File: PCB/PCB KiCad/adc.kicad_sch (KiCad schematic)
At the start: 9 parts, among them U2 NAU7802SGI

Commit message: pre route
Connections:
- net DRDY_INT: no longer names the net of U2.12 (DRDY)
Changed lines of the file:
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@@
   (no_connect (at 163.83 109.22))
   (no_connect (at 163.83 106.68))
-  (wire (pts (xy 163.83 93.98) (xy 175.26 93.98))
-    (stroke (width 0) (type default))
-  )
   (wire (pts (xy 128.27 106.68) (xy 133.35 106.68))
     (stroke (width 0) (type default))
@@
     (stroke (width 0) (type default))
   )
-  (global_label "DRDY_INT" (shape input) (at 175.26 93.98 0) (fields_autoplaced)
-    (effects (font (size 1.27 1.27)) (justify left))
-    (property "Intersheetrefs" "${INTERSHEET_REFS}" (at 186.4421 93.9006 0)
-      (effects (font (size 1.27 1.27)) (justify left) hide)
-    )
-  )
   (global_label "SCL" (shape bidirectional) (at 170.18 99.06 0) (fields_autoplaced)

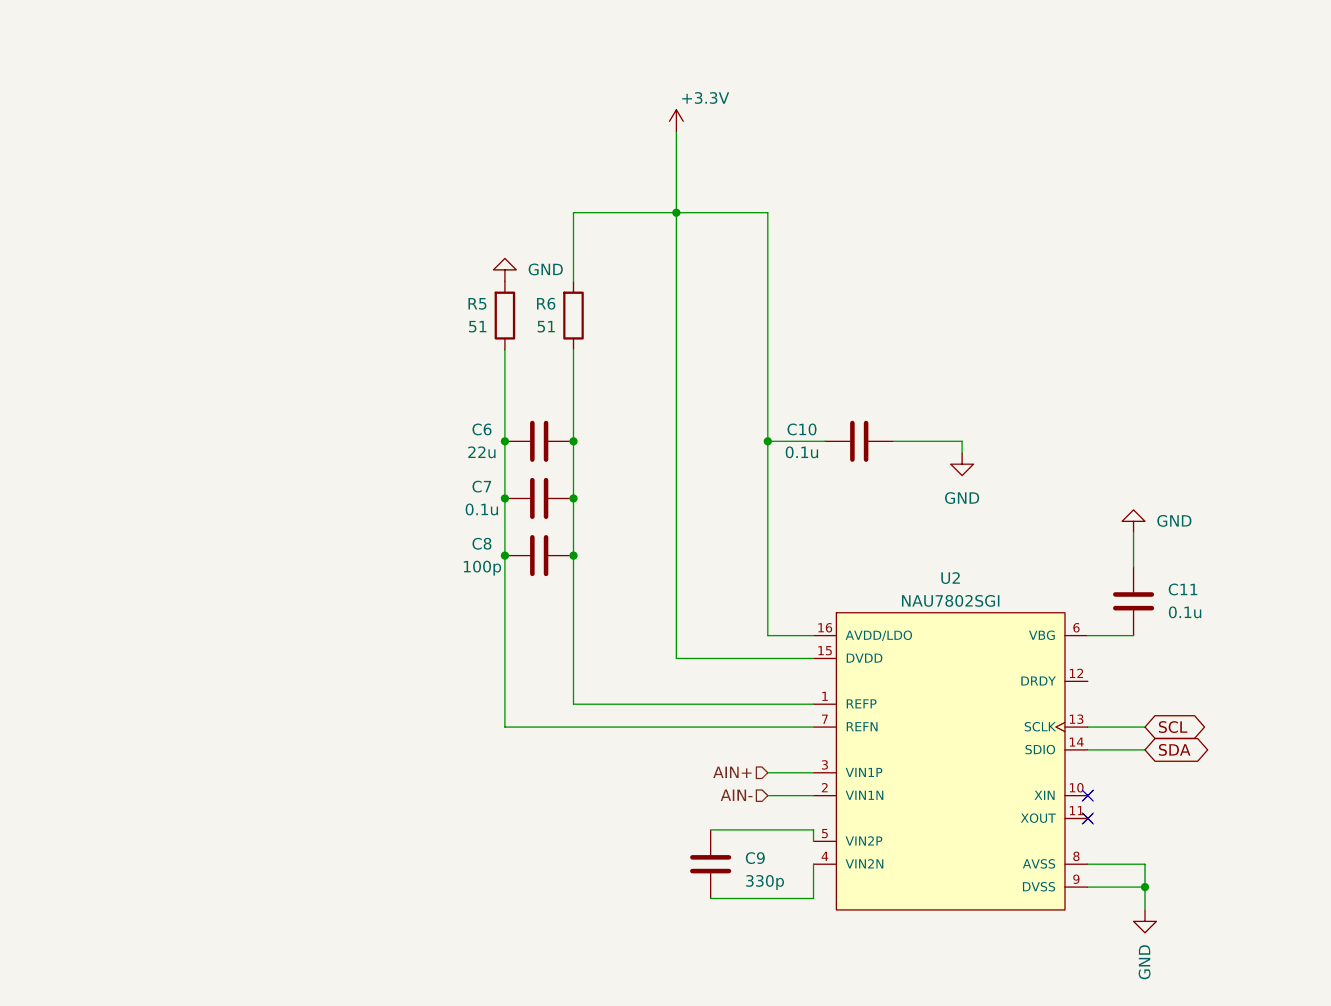
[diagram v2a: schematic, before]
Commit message: adds LP5951MFX
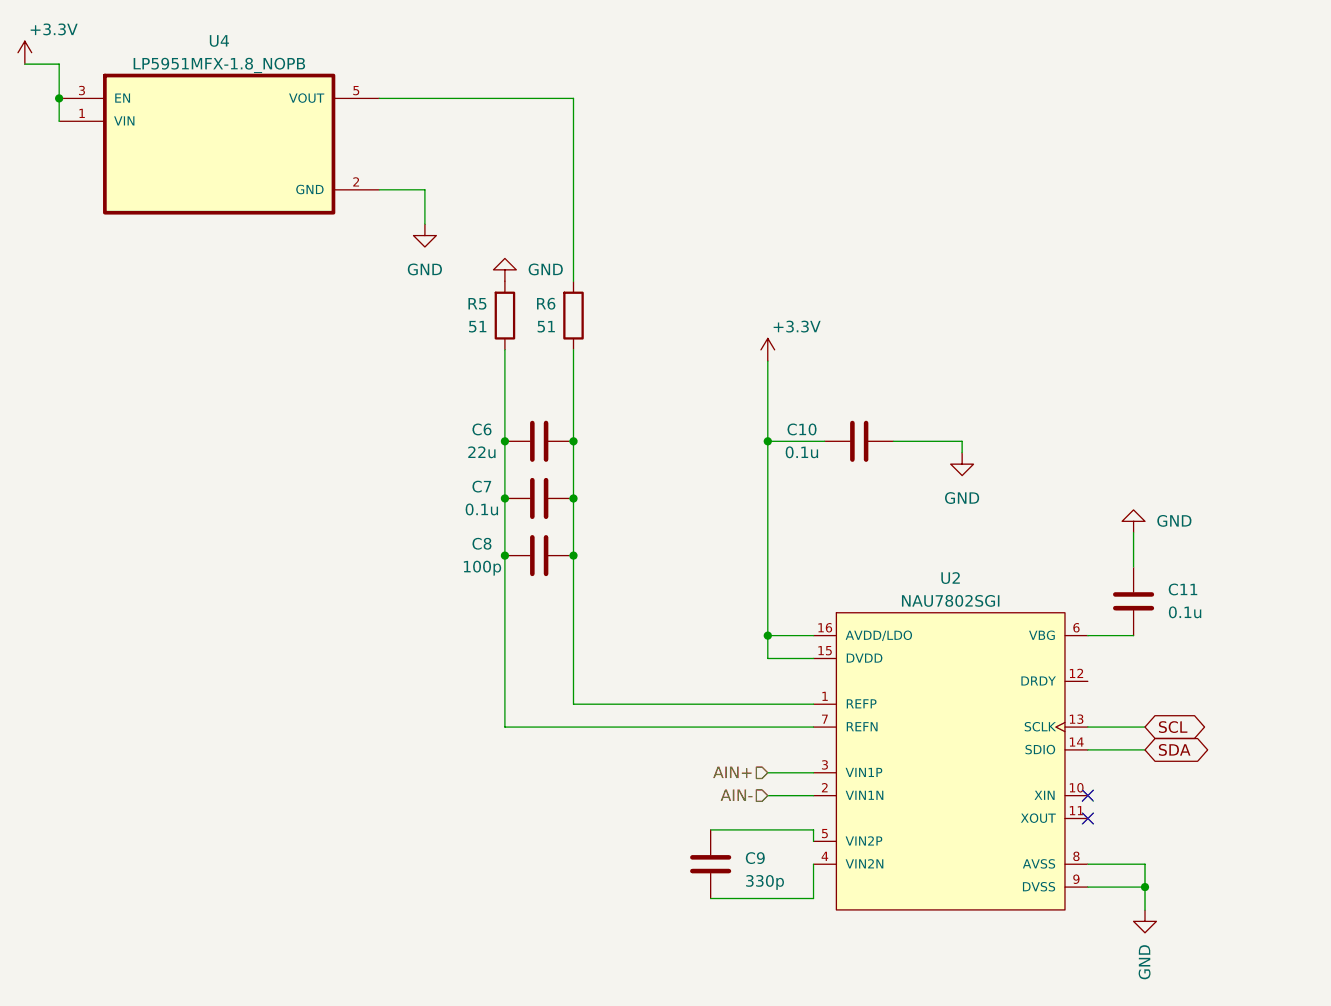
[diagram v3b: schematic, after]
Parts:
- added U4: LP5951MFX-1.8_NOPB, LP5951MFX-1.8_NOPB:SOT95P280X145-5N, symbol LP5951MFX-1.8_NOPB:LP5951MFX-1.8_NOPB
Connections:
- net +3V3: now also U4.1 (VIN), U4.3 (EN); no longer R6.2
- net GND: now also U4.2 (GND)
- new net: R6.2, U4.5 (VOUT)
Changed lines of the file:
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@@
   (junction (at 106.68 67.31) (diameter 0) (color 0 0 0 0)
   )
-  (junction (at 118.11 41.91) (diameter 0) (color 0 0 0 0)
+  (junction (at 49.53 29.21) (diameter 0) (color 0 0 0 0)
+  )
+  (junction (at 128.27 88.9) (diameter 0) (color 0 0 0 0)
   )
   (junction (at 170.18 116.84) (diameter 0) (color 0 0 0 0)
@@
     (stroke (width 0) (type default))
   )
-  (wire (pts (xy 118.11 91.44) (xy 133.35 91.44))
-    (stroke (width 0) (type default))
-  )
-  (wire (pts (xy 118.11 41.91) (xy 118.11 91.44))
+  (wire (pts (xy 90.17 39.37) (xy 90.17 43.18))
+    (stroke (width 0) (type default))
+  )
+  (wire (pts (xy 133.35 88.9) (xy 128.27 88.9))
     (stroke (width 0) (type default))
   )
@@
     (stroke (width 0) (type default))
   )
-  (wire (pts (xy 118.11 33.02) (xy 118.11 41.91))
-    (stroke (width 0) (type default))
-  )
   (wire (pts (xy 163.83 99.06) (xy 170.18 99.06))
     (stroke (width 0) (type default))
   )
+  (wire (pts (xy 128.27 88.9) (xy 128.27 91.44))
+    (stroke (width 0) (type default))
+  )
   (wire (pts (xy 121.92 110.49) (xy 133.35 110.49))
     (stroke (width 0) (type default))
   )
-  (wire (pts (xy 128.27 41.91) (xy 128.27 67.31))
-    (stroke (width 0) (type default))
-  )
-  (wire (pts (xy 106.68 41.91) (xy 106.68 49.53))
-    (stroke (width 0) (type default))
-  )
-  (wire (pts (xy 128.27 88.9) (xy 133.35 88.9))
+  (wire (pts (xy 49.53 25.4) (xy 45.72 25.4))
+    (stroke (width 0) (type default))
+  )
+  (wire (pts (xy 128.27 67.31) (xy 128.27 88.9))
+    (stroke (width 0) (type default))
+  )
+  (wire (pts (xy 128.27 67.31) (xy 134.62 67.31))
+    (stroke (width 0) (type default))
+  )
+  (wire (pts (xy 128.27 58.42) (xy 128.27 67.31))
+    (stroke (width 0) (type default))
+  )
+  (wire (pts (xy 49.53 31.75) (xy 49.53 29.21))
+    (stroke (width 0) (type default))
+  )
+  (wire (pts (xy 133.35 91.44) (xy 128.27 91.44))
     (stroke (width 0) (type default))
   )
@@
     (stroke (width 0) (type default))
   )
-  (wire (pts (xy 134.62 67.31) (xy 128.27 67.31))
+  (wire (pts (xy 85.09 29.21) (xy 106.68 29.21))
     (stroke (width 0) (type default))
   )
@@
     (stroke (width 0) (type default))
   )
+  (wire (pts (xy 85.09 39.37) (xy 90.17 39.37))
+    (stroke (width 0) (type default))
+  )
   (wire (pts (xy 163.83 114.3) (xy 170.18 114.3))
     (stroke (width 0) (type default))
@@
     (stroke (width 0) (type default))
   )
-  (wire (pts (xy 106.68 41.91) (xy 118.11 41.91))
-    (stroke (width 0) (type default))
-  )
-  (wire (pts (xy 128.27 41.91) (xy 118.11 41.91))
+  (wire (pts (xy 49.53 29.21) (xy 49.53 25.4))
     (stroke (width 0) (type default))
   )
@@
     (stroke (width 0) (type default))
   )
-  (wire (pts (xy 128.27 67.31) (xy 128.27 88.9))
+  (wire (pts (xy 106.68 29.21) (xy 106.68 49.53))
     (stroke (width 0) (type default))
   )
@@
         (path "/a818e058-3544-4da8-96fb-1a428660711f/a8dcb7a4-48cf-403e-b881-d44234291c62"
           (reference "C7") (unit 1)
+        )
+      )
+    )
+  )
+  (symbol (lib_id "LP5951MFX-1.8_NOPB:LP5951MFX-1.8_NOPB") (at 67.31 34.29 0) (unit 1)
+    (in_bom yes) (on_board yes) (dnp no) (fields_autoplaced)
+    (property "Reference" "U4" (at 67.31 22.86 0)
+      (effects (font (size 1.27 1.27)))
+    )
+    (property "Value" "LP5951MFX-1.8_NOPB" (at 67.31 25.4 0)
+      (effects (font (size 1.27 1.27)))
+    )
+    (property "Footprint" "LP5951MFX-1.8_NOPB:SOT95P280X145-5N" (at 71.12 21.59 0)
+      (effects (font (size 1.27 1.27)) (justify bottom) hide)
+    )
+    (property "Datasheet" "" (at 67.31 34.29 0)
+      (effects (font (size 1.27 1.27)) hide)
+    )
+    (property "MF" " " (at 48.26 36.83 0)
+      (effects (font (size 1.27 1.27)) (justify bottom) hide)
+    )
+    (property "Description" " " (at 67.31 34.29 0)
+      (effects (font (size 1.27 1.27)) (justify bottom) hide)
+    )
+    (property "Package" "" (at 49.53 44.45 0)
+      (effects (font (size 1.27 1.27)) (justify bottom) hide)
+    )
+    (property "Price" "" (at 62.23 25.4 0)
+      (effects (font (size 1.27 1.27)) (justify bottom) hide)
+    )
+    (property "SnapEDA_Link" "" (at 67.31 34.29 0)
+      (effects (font (size 1.27 1.27)) (justify bottom) hide)
+    )
+    (property "MP" "" (at 82.55 38.1 0)
+      (effects (font (size 1.27 1.27)) (justify bottom) hide)
+    )
+    (property "Purchase-URL" " " (at 67.31 34.29 0)
+      (effects (font (size 1.27 1.27)) (justify bottom) hide)
+    )
+    (property "Availability" "" (at 64.77 17.78 0)
+      (effects (font (size 1.27 1.27)) (justify bottom) hide)
+    )
+    (property "Check_prices" " " (at 67.31 34.29 0)
+      (effects (font (size 1.27 1.27)) (justify bottom) hide)
+    )
+    (pin "1")
+    (pin "2")
+    (pin "3")
+    (pin "5")
+    (instances
+      (project "PCB KiCad"
+        (path "/a818e058-3544-4da8-96fb-1a428660711f/a8dcb7a4-48cf-403e-b881-d44234291c62"
+          (reference "U4") (unit 1)
         )
       )
@@
     )
   )
-  (symbol (lib_id "power:+3.3V") (at 118.11 33.02 0) (unit 1)
+  (symbol (lib_id "power:GND") (at 90.17 43.18 0) (unit 1)
+    (in_bom yes) (on_board yes) (dnp no) (fields_autoplaced)
+    (property "Reference" "#PWR020" (at 90.17 49.53 0)
+      (effects (font (size 1.27 1.27)) hide)
+    )
+    (property "Value" "GND" (at 90.17 48.26 0)
+      (effects (font (size 1.27 1.27)))
+    )
+    (property "Footprint" "" (at 90.17 43.18 0)
+      (effects (font (size 1.27 1.27)) hide)
+    )
+    (property "Datasheet" "" (at 90.17 43.18 0)
+      (effects (font (size 1.27 1.27)) hide)
+    )
+    (pin "1")
+    (instances
+      (project "PCB KiCad"
+        (path "/a818e058-3544-4da8-96fb-1a428660711f/a8dcb7a4-48cf-403e-b881-d44234291c62"
+          (reference "#PWR020") (unit 1)
+        )
+      )
+    )
+  )
+  (symbol (lib_id "power:+3.3V") (at 45.72 25.4 0) (unit 1)
     (in_bom yes) (on_board yes) (dnp no)
-    (property "Reference" "#PWR06" (at 118.11 36.83 0)
-      (effects (font (size 1.27 1.27)) hide)
-    )
-    (property "Value" "+3.3V" (at 121.285 29.21 0)
-      (effects (font (size 1.27 1.27)))
-    )
-    (property "Footprint" "" (at 118.11 33.02 0)
-      (effects (font (size 1.27 1.27)) hide)
-    )
-    (property "Datasheet" "" (at 118.11 33.02 0)
-      (effects (font (size 1.27 1.27)) hide)
-    )
+    (property "Reference" "#PWR021" (at 45.72 29.21 0)
+      (effects (font (size 1.27 1.27)) hide)
+    )
+    (property "Value" "+3.3V" (at 48.895 21.59 0)
+      (effects (font (size 1.27 1.27)))
+    )
+    (property "Footprint" "" (at 45.72 25.4 0)
+      (effects (font (size 1.27 1.27)) hide)
+    )
+    (property "Datasheet" "" (at 45.72 25.4 0)
+      (effects (font (size 1.27 1.27)) hide)
+    )
+    (pin "1")
+    (instances
+      (project "PCB KiCad"
+        (path "/a818e058-3544-4da8-96fb-1a428660711f/a8dcb7a4-48cf-403e-b881-d44234291c62"
+          (reference "#PWR021") (unit 1)
+        )
+      )
+    )
+  )
+  (symbol (lib_id "power:+3.3V") (at 128.27 58.42 0) (unit 1)
+    (in_bom yes) (on_board yes) (dnp no)
+    (property "Reference" "#PWR06" (at 128.27 62.23 0)
+      (effects (font (size 1.27 1.27)) hide)
+    )
+    (property "Value" "+3.3V" (at 131.445 54.61 0)
+      (effects (font (size 1.27 1.27)))
+    )
+    (property "Footprint" "" (at 128.27 58.42 0)
+      (effects (font (size 1.27 1.27)) hide)
+    )
+    (property "Datasheet" "" (at 128.27 58.42 0)
+      (effects (font (size 1.27 1.27)) hide)
+    )
